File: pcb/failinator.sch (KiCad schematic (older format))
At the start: 3 parts, among them P1 CONN_01X04, P4 CONN_01X06, U2 RASPIPLUSHEADER

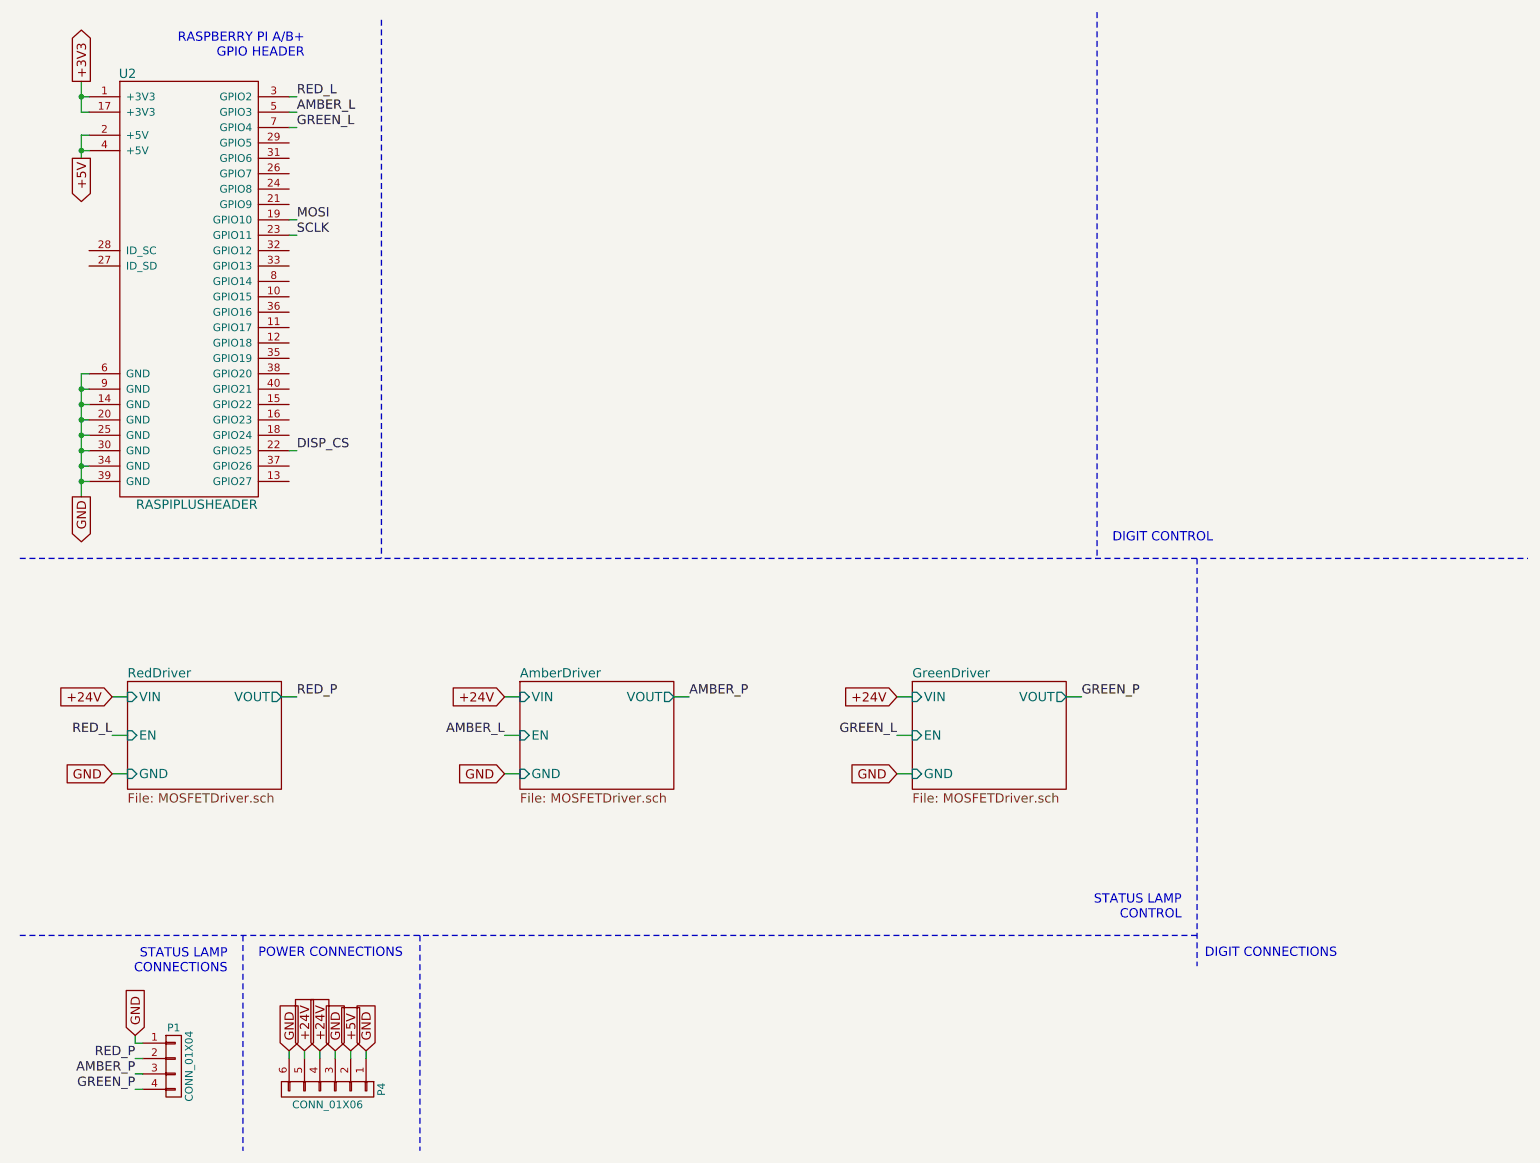
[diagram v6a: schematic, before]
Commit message: Squeeze schematic layout to make more space.
The 7 segment LED driver sub-circuits are going to take up a bunch of
space.
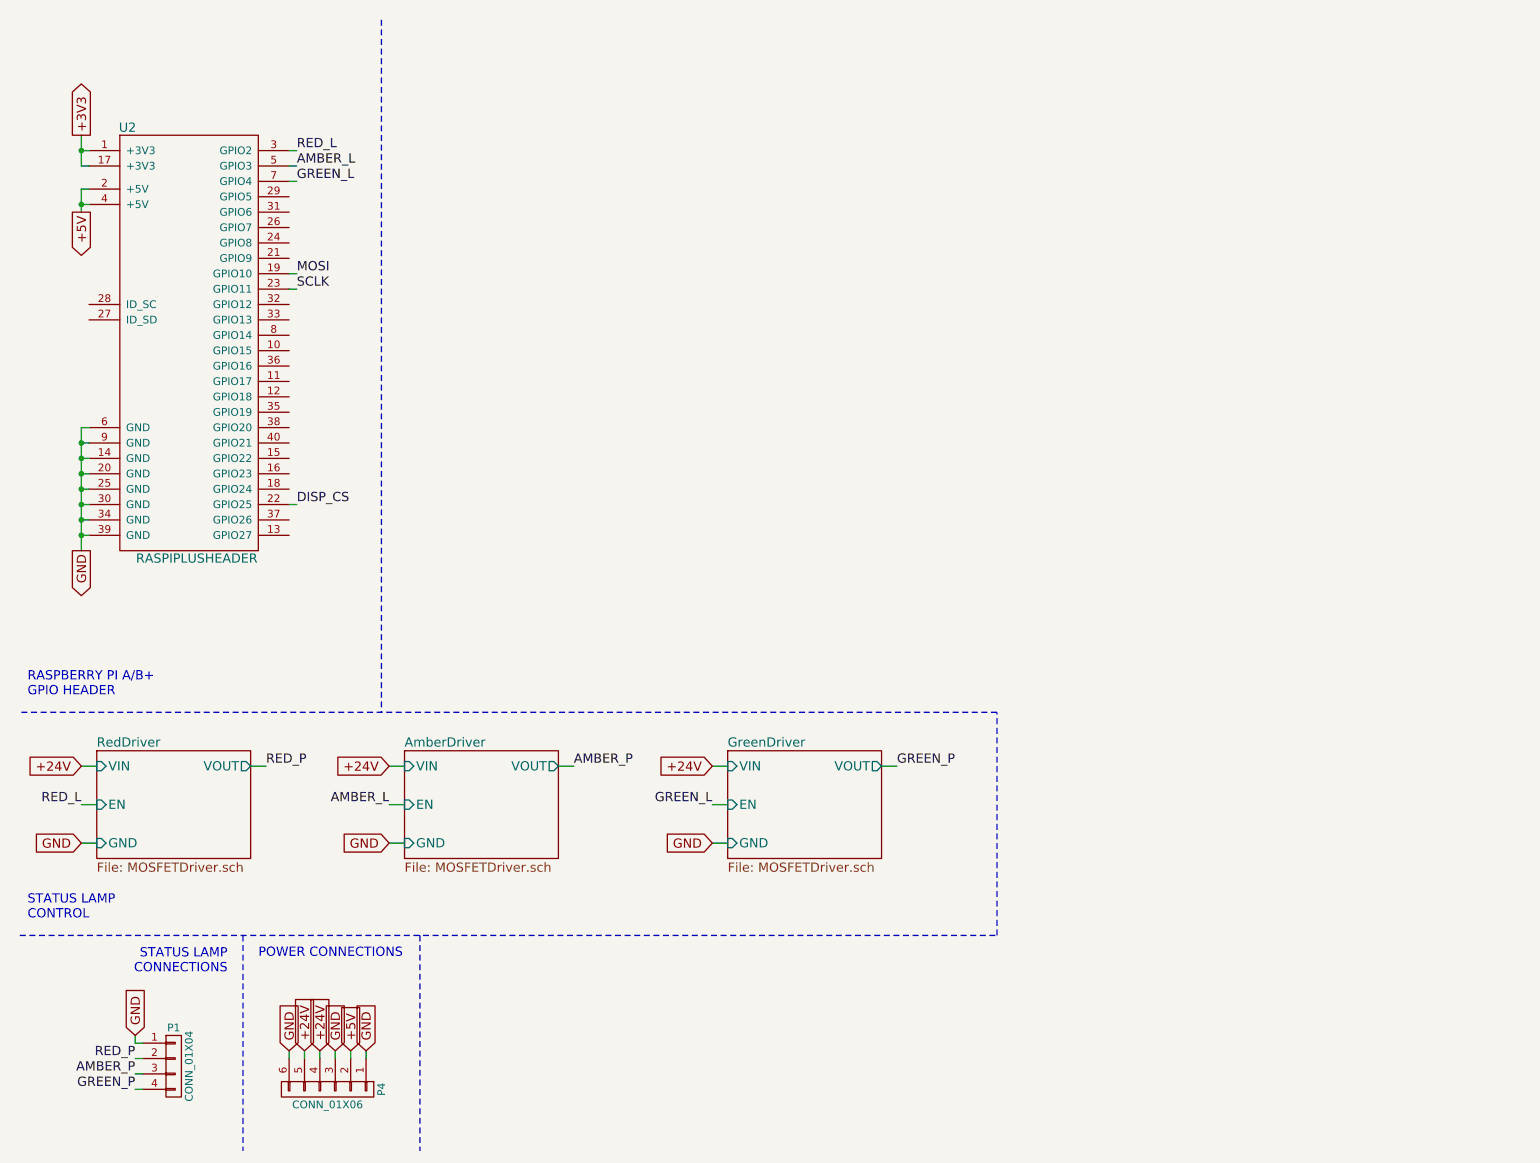
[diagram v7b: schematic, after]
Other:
- note removed: "DIGIT CONNECTIONS"
- note removed: "DIGIT CONTROL"
- moved on the sheet: U2
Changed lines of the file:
@@
 L RASPIPLUSHEADER U2
 U 1 1 54A79B4A
-P 1700 2300
-F 0 "U2" H 1300 3650 60  0000 C CNN
-F 1 "RASPIPLUSHEADER" H 1750 850 60  0000 C CNN
-F 2 "Pin_Headers:Pin_Header_Straight_2x20" H 1700 2050 60  0001 C CNN
-F 3 "" H 1700 2050 60  0000 C CNN
-	1    1700 2300
+P 1700 2650
+F 0 "U2" H 1300 4000 60  0000 C CNN
+F 1 "RASPIPLUSHEADER" H 1750 1200 60  0000 C CNN
+F 2 "Pin_Headers:Pin_Header_Straight_2x20" H 1700 2400 60  0001 C CNN
+F 3 "" H 1700 2400 60  0000 C CNN
+	1    1700 2650
 	1    0    0    -1
 $EndComp
-Text GLabel 1000 3700 3    60   Output ~ 0
-GND
-Text GLabel 1000 1000 1    60   Output ~ 0
+Text GLabel 1000 4050 3    60   Output ~ 0
+GND
+Text GLabel 1000 1350 1    60   Output ~ 0
 +3V3
 Wire Wire Line
-	1050 2900 1000 2900
-Wire Wire Line
-	1000 2900 1000 3700
-Wire Wire Line
-	1050 3000 1000 3000
-Connection ~ 1000 3000
-Wire Wire Line
-	1050 3100 1000 3100
-Connection ~ 1000 3100
-Wire Wire Line
-	1050 3200 1000 3200
-Connection ~ 1000 3200
-Wire Wire Line
-	1050 3300 1000 3300
-Connection ~ 1000 3300
-Wire Wire Line
-	1050 3400 1000 3400
-Connection ~ 1000 3400
-Wire Wire Line
-	1050 3500 1000 3500
-Connection ~ 1000 3500
-Wire Wire Line
-	1050 3600 1000 3600
-Connection ~ 1000 3600
-Wire Wire Line
-	1000 1000 1000 1200
-Wire Wire Line
-	1000 1200 1050 1200
-Wire Wire Line
-	1050 1100 1000 1100
-Connection ~ 1000 1100
-Text Notes 2450 850  2    60   ~ 0
-RASPBERRY PI A/B+\nGPIO HEADER
-Text GLabel 1000 1500 3    60   Output ~ 0
-+5V
-Wire Wire Line
-	1050 1350 1000 1350
-Wire Wire Line
-	1000 1350 1000 1500
+	1050 3250 1000 3250
+Wire Wire Line
+	1000 3250 1000 4050
+Wire Wire Line
+	1050 3350 1000 3350
+Connection ~ 1000 3350
+Wire Wire Line
+	1050 3450 1000 3450
+Connection ~ 1000 3450
+Wire Wire Line
+	1050 3550 1000 3550
+Connection ~ 1000 3550
+Wire Wire Line
+	1050 3650 1000 3650
+Connection ~ 1000 3650
+Wire Wire Line
+	1050 3750 1000 3750
+Connection ~ 1000 3750
+Wire Wire Line
+	1050 3850 1000 3850
+Connection ~ 1000 3850
+Wire Wire Line
+	1050 3950 1000 3950
+Connection ~ 1000 3950
+Wire Wire Line
+	1000 1350 1000 1550
+Wire Wire Line
+	1000 1550 1050 1550
 Wire Wire Line
 	1050 1450 1000 1450
 Connection ~ 1000 1450
-Text Label 2400 1900 0    60   ~ 0
+Text Notes 650  5000 0    60   ~ 0
+RASPBERRY PI A/B+\nGPIO HEADER
+Text GLabel 1000 1850 3    60   Output ~ 0
++5V
+Wire Wire Line
+	1050 1700 1000 1700
+Wire Wire Line
+	1000 1700 1000 1850
+Wire Wire Line
+	1050 1800 1000 1800
+Connection ~ 1000 1800
+Text Label 2400 2250 0    60   ~ 0
 MOSI
-Text Label 2400 2000 0    60   ~ 0
+Text Label 2400 2350 0    60   ~ 0
 SCLK
 Wire Wire Line
-	2350 1900 2400 1900
-Wire Wire Line
-	2350 2000 2400 2000
-Text Label 2400 3400 0    60   ~ 0
+	2350 2250 2400 2250
+Wire Wire Line
+	2350 2350 2400 2350
+Text Label 2400 3750 0    60   ~ 0
 DISP_CS
 Wire Wire Line
-	2350 3400 2400 3400
-Text Label 2400 1100 0    60   ~ 0
+	2350 3750 2400 3750
+Text Label 2400 1450 0    60   ~ 0
 RED_L
-Text Label 2400 1200 0    60   ~ 0
+Text Label 2400 1550 0    60   ~ 0
 AMBER_L
-Text Label 2400 1300 0    60   ~ 0
+Text Label 2400 1650 0    60   ~ 0
 GREEN_L
 Wire Wire Line
-	2350 1100 2400 1100
-Wire Wire Line
-	2350 1200 2400 1200
-Wire Wire Line
-	2350 1300 2400 1300
+	2350 1450 2400 1450
+Wire Wire Line
+	2350 1550 2400 1550
+Wire Wire Line
+	2350 1650 2400 1650
 $Comp
 L CONN_01X04 P1
@@
 Wire Wire Line
 	1350 7550 1400 7550
-Text GLabel 1200 5500 0    60   Input ~ 0
-GND
-Text GLabel 1200 5000 0    60   Input ~ 0
-+24V
-Text Label 1200 5250 2    60   ~ 0
+Text GLabel 1000 5950 0    60   Input ~ 0
+GND
+Text GLabel 1000 5450 0    60   Input ~ 0
++24V
+Text Label 1000 5700 2    60   ~ 0
 RED_L
-Text Label 2400 5000 0    60   ~ 0
+Text Label 2200 5450 0    60   ~ 0
 RED_P
-Text GLabel 3750 5500 0    60   Input ~ 0
-GND
-Text GLabel 3750 5000 0    60   Input ~ 0
-+24V
-Text Label 3750 5250 2    60   ~ 0
+Text GLabel 3000 5950 0    60   Input ~ 0
+GND
+Text GLabel 3000 5450 0    60   Input ~ 0
++24V
+Text Label 3000 5700 2    60   ~ 0
 AMBER_L
-Text Label 4950 5000 0    60   ~ 0
+Text Label 4200 5450 0    60   ~ 0
 AMBER_P
-Text GLabel 6300 5500 0    60   Input ~ 0
-GND
-Text GLabel 6300 5000 0    60   Input ~ 0
-+24V
-Text Label 6300 5250 2    60   ~ 0
+Text GLabel 5100 5950 0    60   Input ~ 0
+GND
+Text GLabel 5100 5450 0    60   Input ~ 0
++24V
+Text Label 5100 5700 2    60   ~ 0
 GREEN_L
-Text Label 7500 5000 0    60   ~ 0
+Text Label 6300 5450 0    60   ~ 0
 GREEN_P
 Wire Notes Line
-	2950 600  2950 4100
-Wire Notes Line
-	600  4100 10400 4100
-Wire Notes Line
-	8250 4100 8250 6750
-Wire Notes Line
-	8250 6550 600  6550
-Wire Notes Line
 	2050 6550 2050 7950
-Wire Notes Line
-	7600 550  7600 4100
-Text Notes 7700 4000 0    60   ~ 0
-DIGIT CONTROL
-Text Notes 8300 6700 0    60   ~ 0
-DIGIT CONNECTIONS
 Text Notes 1950 6800 2    60   ~ 0
 STATUS LAMP\nCONNECTIONS
-Text Notes 8150 6450 2    60   ~ 0
+Text Notes 650  6450 0    60   ~ 0
 STATUS LAMP\nCONTROL
 $Comp
@@
 POWER CONNECTIONS
 $Sheet
-S 1300 4900 1000 700
+S 1100 5350 1000 700
 U 568778A1
 F0 "RedDriver" 60
 F1 "MOSFETDriver.sch" 60
-F2 "VIN" I L 1300 5000 60
-F3 "GND" I L 1300 5500 60
-F4 "EN" I L 1300 5250 60
-F5 "VOUT" O R 2300 5000 60
+F2 "VIN" I L 1100 5450 60
+F3 "GND" I L 1100 5950 60
+F4 "EN" I L 1100 5700 60
+F5 "VOUT" O R 2100 5450 60
 $EndSheet
 Wire Wire Line
-	2300 5000 2400 5000
-Wire Wire Line
-	1200 5000 1300 5000
-Wire Wire Line
-	1200 5250 1300 5250
-Wire Wire Line
-	1200 5500 1300 5500
+	2100 5450 2200 5450
+Wire Wire Line
+	1000 5450 1100 5450
+Wire Wire Line
+	1000 5700 1100 5700
+Wire Wire Line
+	1000 5950 1100 5950
 $Sheet
-S 3850 4900 1000 700
+S 3100 5350 1000 700
 U 56879543
 F0 "AmberDriver" 60
 F1 "MOSFETDriver.sch" 60
-F2 "VIN" I L 3850 5000 60
-F3 "GND" I L 3850 5500 60
-F4 "EN" I L 3850 5250 60
-F5 "VOUT" O R 4850 5000 60
+F2 "VIN" I L 3100 5450 60
+F3 "GND" I L 3100 5950 60
+F4 "EN" I L 3100 5700 60
+F5 "VOUT" O R 4100 5450 60
 $EndSheet
 $Sheet
-S 6400 4900 1000 700
+S 5200 5350 1000 700
 U 5687AB7C
 F0 "GreenDriver" 60
 F1 "MOSFETDriver.sch" 60
-F2 "VIN" I L 6400 5000 60
-F3 "GND" I L 6400 5500 60
-F4 "EN" I L 6400 5250 60
-F5 "VOUT" O R 7400 5000 60
+F2 "VIN" I L 5200 5450 60
+F3 "GND" I L 5200 5950 60
+F4 "EN" I L 5200 5700 60
+F5 "VOUT" O R 6200 5450 60
 $EndSheet
 Wire Wire Line
-	3750 5000 3850 5000
-Wire Wire Line
-	3750 5250 3850 5250
-Wire Wire Line
-	3750 5500 3850 5500
-Wire Wire Line
-	4850 5000 4950 5000
-Wire Wire Line
-	6300 5000 6400 5000
-Wire Wire Line
-	6300 5250 6400 5250
-Wire Wire Line
-	6300 5500 6400 5500
-Wire Wire Line
-	7400 5000 7500 5000
+	3000 5450 3100 5450
+Wire Wire Line
+	3000 5700 3100 5700
+Wire Wire Line
+	3000 5950 3100 5950
+Wire Wire Line
+	4100 5450 4200 5450
+Wire Wire Line
+	5100 5450 5200 5450
+Wire Wire Line
+	5100 5700 5200 5700
+Wire Wire Line
+	5100 5950 5200 5950
+Wire Wire Line
+	6200 5450 6300 5450
+Wire Notes Line
+	600  6550 6950 6550
+Wire Notes Line
+	6950 6550 6950 5100
+Wire Notes Line
+	6950 5100 600  5100
+Wire Notes Line
+	2950 600  2950 5100
 $EndSCHEMATC

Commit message: 7-segment LED displays and their ground connections
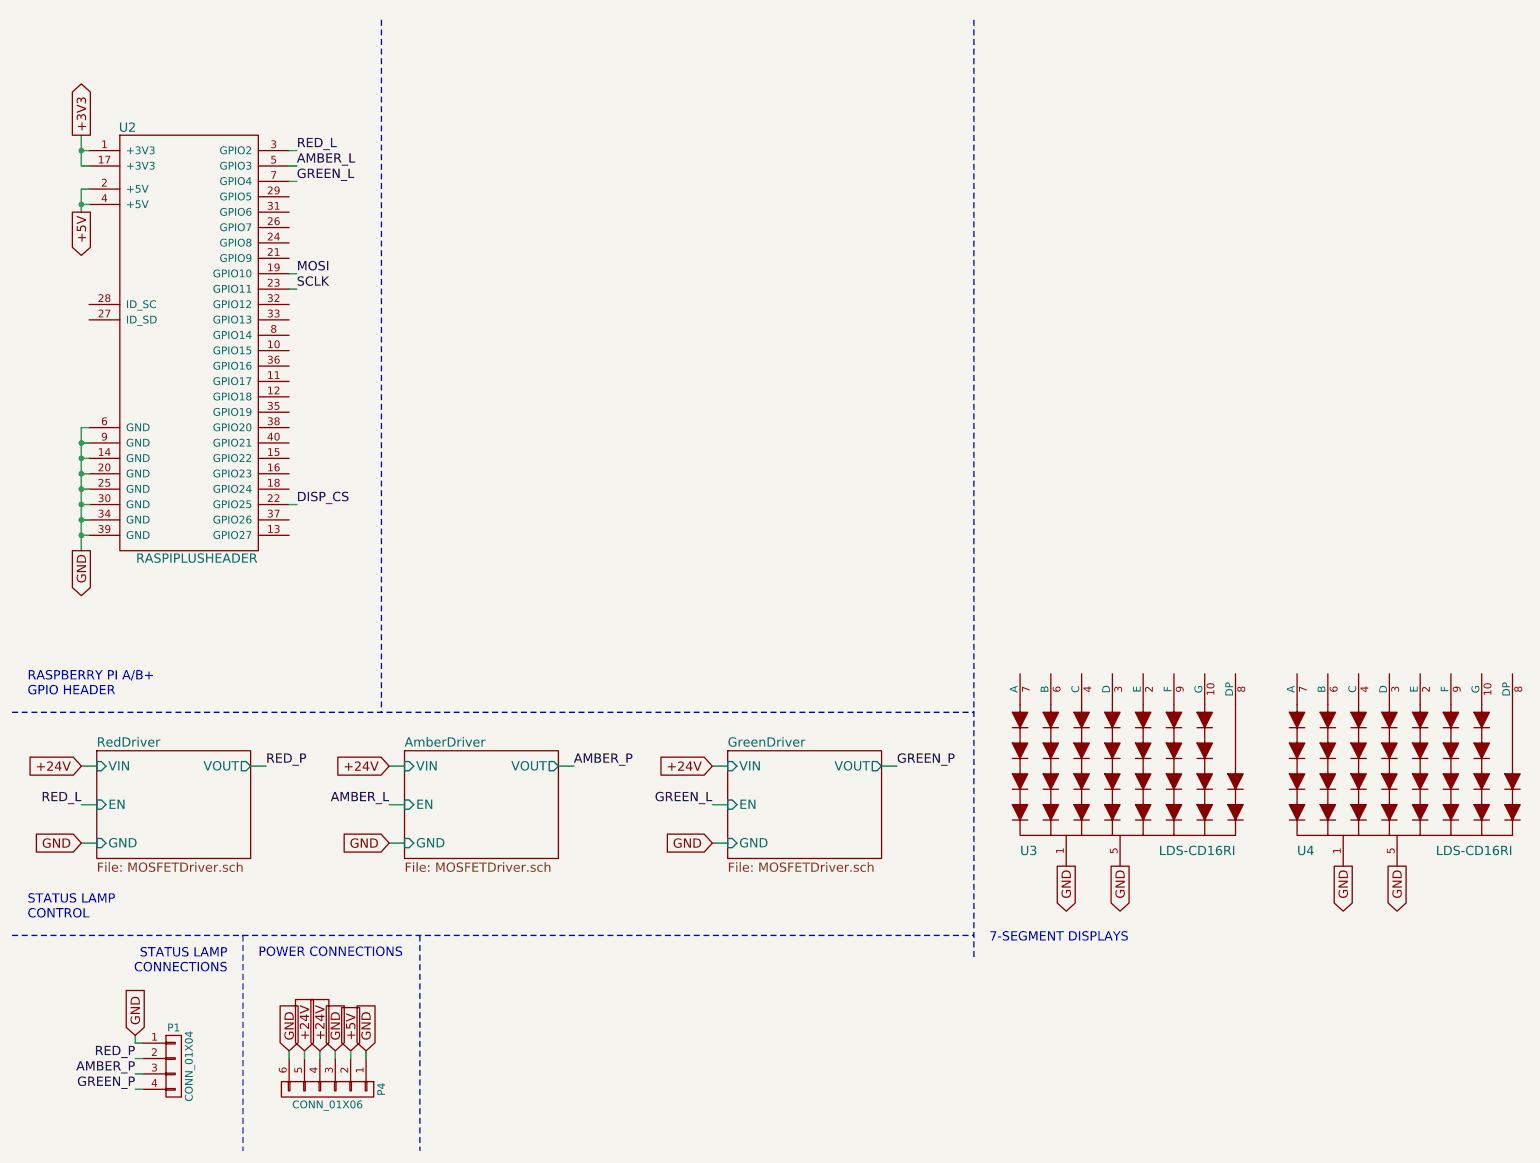
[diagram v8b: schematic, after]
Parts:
- added U3, U4: LDS-CD16RI, symbol LDS-CD16RI
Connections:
- net GND: now also U3.1, U3.5, U4.1, U4.5
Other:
- note added: "7-SEGMENT DISPLAYS"
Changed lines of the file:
@@
 	6200 5450 6300 5450
 Wire Notes Line
-	600  6550 6950 6550
+	2950 600  2950 5100
+$Comp
+L LDS-CD16RI U3
+U 1 1 5688764B
+P 7800 5450
+F 0 "U3" H 7100 4900 60  0000 L CNN
+F 1 "LDS-CD16RI" H 8500 4900 60  0000 R CNN
+F 2 "" H 7550 5850 60  0000 C CNN
+F 3 "" H 7550 5850 60  0000 C CNN
+	1    7800 5450
+	1    0    0    -1
+$EndComp
+Text GLabel 7400 6100 3    60   Output ~ 0
+GND
+Text GLabel 7750 6100 3    60   Output ~ 0
+GND
+$Comp
+L LDS-CD16RI U4
+U 1 1 56887D47
+P 9600 5450
+F 0 "U4" H 8900 4900 60  0000 L CNN
+F 1 "LDS-CD16RI" H 10300 4900 60  0000 R CNN
+F 2 "" H 9350 5850 60  0000 C CNN
+F 3 "" H 9350 5850 60  0000 C CNN
+	1    9600 5450
+	1    0    0    -1
+$EndComp
+Text GLabel 9200 6100 3    60   Output ~ 0
+GND
+Text GLabel 9550 6100 3    60   Output ~ 0
+GND
+Text Notes 6900 6600 0    60   ~ 0
+7-SEGMENT DISPLAYS
 Wire Notes Line
-	6950 6550 6950 5100
+	550  6550 6800 6550
 Wire Notes Line
-	6950 5100 600  5100
+	6800 600  6800 6700
 Wire Notes Line
-	2950 600  2950 5100
+	550  5100 6800 5100
 $EndSCHEMATC
